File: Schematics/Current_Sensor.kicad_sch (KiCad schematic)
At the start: 4 parts, among them Q1 INA180A2

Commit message: finished and ERC schematic
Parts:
- C1: renamed from C4; value 100nF -> 100nf; LCSC (none) -> C49678
- C2: renamed from C5; value 100nF -> 100nf; LCSC (none) -> C49678
- Q1: LCSC (none) -> C192764
- R1: renamed from R4; LCSC (none) -> C114523
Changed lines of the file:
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@@
 		(dnp no)
 		(fields_autoplaced yes)
-		(property "Reference" "C4"
+		(property "Reference" "C1"
 			(at 132.08 83.8199 0)
 			(effects
@@
 			)
 		)
-		(property "Value" "100nF"
+		(property "Value" "100nf"
 			(at 132.08 86.3599 0)
 			(effects
@@
 			)
 		)
+		(property "LCSC" "C49678"
+			(at 128.27 85.09 0)
+			(effects
+				(font
+					(size 1.27 1.27)
+				)
+				(hide yes)
+			)
+		)
 		(pin "1"
 		)
@@
 			(project "CAN-Interface-Board"
 				(path "/8a3e7f99-4046-40e8-bd7c-d9d1c8c7162e/15bd7aa7-9f9b-43b9-8a5d-de3a8ae7f7af"
-					(reference "C4")
+					(reference "C1")
 					(unit 1)
 				)
@@
 		(dnp no)
 		(fields_autoplaced yes)
-		(property "Reference" "#PWR02"
+		(property "Reference" "#PWR03"
 			(at 149.86 69.85 0)
 			(effects
@@
 			(project ""
 				(path "/8a3e7f99-4046-40e8-bd7c-d9d1c8c7162e/15bd7aa7-9f9b-43b9-8a5d-de3a8ae7f7af"
-					(reference "#PWR02")
+					(reference "#PWR03")
 					(unit 1)
 				)
@@
 		(dnp no)
 		(fields_autoplaced yes)
-		(property "Reference" "C5"
+		(property "Reference" "C2"
 			(at 158.75 63.5 90)
 			(effects
@@
 			)
 		)
-		(property "Value" "100nF"
+		(property "Value" "100nf"
 			(at 158.75 66.04 90)
 			(effects
@@
 			)
 		)
+		(property "LCSC" "C49678"
+			(at 158.75 71.12 90)
+			(effects
+				(font
+					(size 1.27 1.27)
+				)
+				(hide yes)
+			)
+		)
 		(pin "1"
 		)
@@
 			(project "CAN-Interface-Board"
 				(path "/8a3e7f99-4046-40e8-bd7c-d9d1c8c7162e/15bd7aa7-9f9b-43b9-8a5d-de3a8ae7f7af"
-					(reference "C5")
+					(reference "C2")
 					(unit 1)
 				)
@@
 		(dnp no)
 		(fields_autoplaced yes)
-		(property "Reference" "#PWR03"
+		(property "Reference" "#PWR05"
 			(at 171.45 77.47 0)
 			(effects
@@
 			(project ""
 				(path "/8a3e7f99-4046-40e8-bd7c-d9d1c8c7162e/15bd7aa7-9f9b-43b9-8a5d-de3a8ae7f7af"
-					(reference "#PWR03")
+					(reference "#PWR05")
 					(unit 1)
 				)
@@
 			)
 		)
+		(property "LCSC" "C192764"
+			(at 152.4 83.82 0)
+			(effects
+				(font
+					(size 1.27 1.27)
+				)
+				(hide yes)
+			)
+		)
 		(pin "3"
 		)
@@
 		(dnp no)
 		(fields_autoplaced yes)
-		(property "Reference" "#PWR01"
+		(property "Reference" "#PWR04"
 			(at 149.86 97.79 0)
 			(effects
@@
 			(project ""
 				(path "/8a3e7f99-4046-40e8-bd7c-d9d1c8c7162e/15bd7aa7-9f9b-43b9-8a5d-de3a8ae7f7af"
-					(reference "#PWR01")
+					(reference "#PWR04")
 					(unit 1)
 				)
@@
 		(dnp no)
 		(fields_autoplaced yes)
-		(property "Reference" "#PWR020"
+		(property "Reference" "#PWR02"
 			(at 109.22 91.44 0)
 			(effects
@@
 			(project ""
 				(path "/8a3e7f99-4046-40e8-bd7c-d9d1c8c7162e/15bd7aa7-9f9b-43b9-8a5d-de3a8ae7f7af"
-					(reference "#PWR020")
+					(reference "#PWR02")
 					(unit 1)
 				)
@@
 		(dnp no)
 		(fields_autoplaced yes)
-		(property "Reference" "#PWR07"
+		(property "Reference" "#PWR01"
 			(at 109.22 81.28 0)
 			(effects
@@
 			(project "CAN-Interface-Board"
 				(path "/8a3e7f99-4046-40e8-bd7c-d9d1c8c7162e/15bd7aa7-9f9b-43b9-8a5d-de3a8ae7f7af"
-					(reference "#PWR07")
+					(reference "#PWR01")
 					(unit 1)
 				)
@@
 		(dnp no)
 		(fields_autoplaced yes)
-		(property "Reference" "R4"
+		(property "Reference" "R1"
 			(at 114.3 85.0899 0)
 			(effects
@@
 			)
 		)
+		(property "LCSC" "C114523"
+			(at 111.76 86.36 0)
+			(effects
+				(font
+					(size 1.27 1.27)
+				)
+				(hide yes)
+			)
+		)
 		(pin "2"
 		)
@@
 			(project ""
 				(path "/8a3e7f99-4046-40e8-bd7c-d9d1c8c7162e/15bd7aa7-9f9b-43b9-8a5d-de3a8ae7f7af"
-					(reference "R4")
-					(unit 1)
-				)
+					(reference "R1")
+					(unit 1)
+				)

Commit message: inital layout started, refining stage
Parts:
- R1: footprint Resistor_SMD:R_1206_3216Metric -> Resistor_SMD:R_0805_2012Metric_Pad1.20x1.40mm_HandSolder
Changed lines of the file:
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@@
 			)
 		)
-		(property "Footprint" "Resistor_SMD:R_1206_3216Metric"
+		(property "Footprint" "Resistor_SMD:R_0805_2012Metric_Pad1.20x1.40mm_HandSolder"
 			(at 109.982 86.36 90)
 			(effects

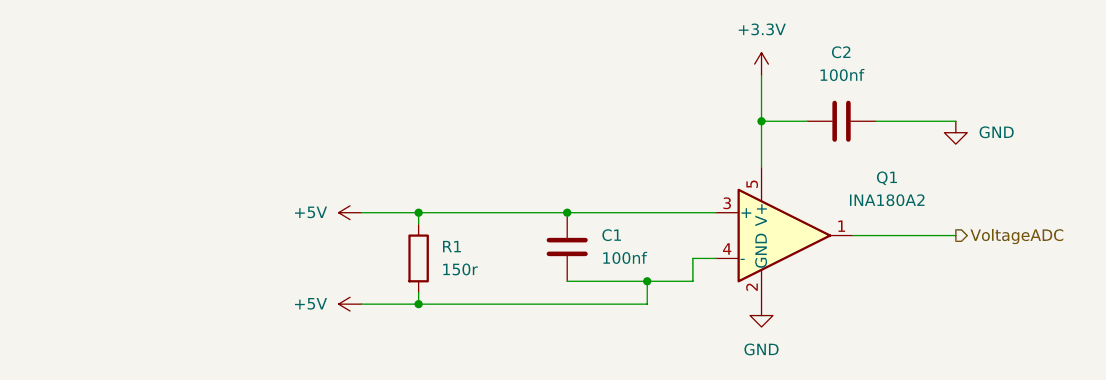
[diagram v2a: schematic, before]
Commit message: put note to fix nets on current sensor
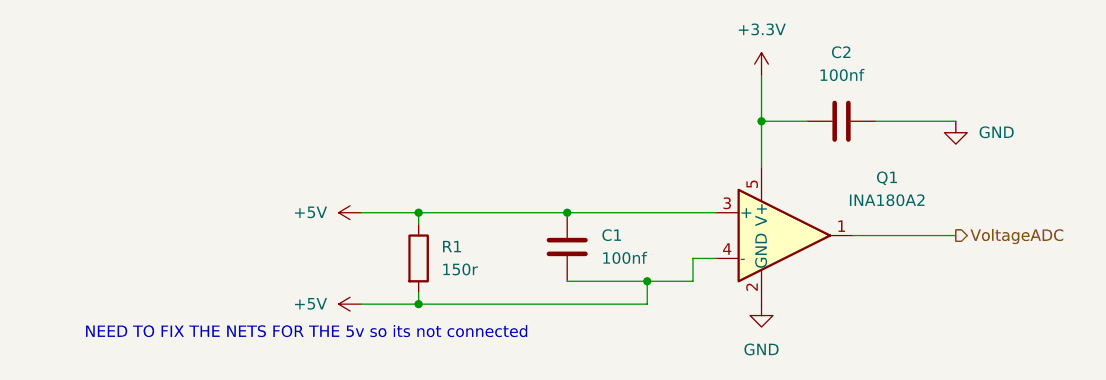
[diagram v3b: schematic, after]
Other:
- note added: "NEED TO FIX THE NETS FOR THE 5v so its not connected"
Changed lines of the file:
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@@
 	(generator_version "9.0")
 	(paper "A4")
+	(text "NEED TO FIX THE NETS FOR THE 5v so its not connected\n"
+		(exclude_from_sim no)
+		(at 99.314 94.742 0)
+		(effects
+			(font
+				(size 1.27 1.27)
+			)
+		)
+	)
 	(junction
 		(at 128.27 81.28)
